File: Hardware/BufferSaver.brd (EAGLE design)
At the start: 12.7 x 17.4 mm, 26 parts, among them U1 SN74AHC1G125, U3 SN74AHC1G125

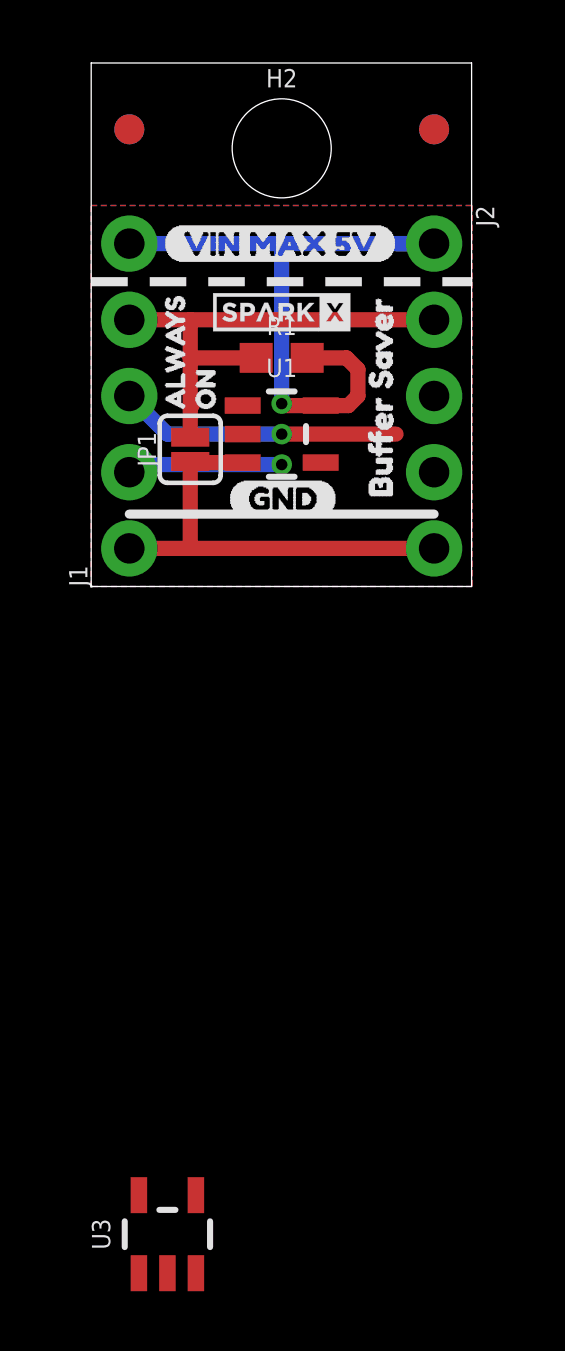
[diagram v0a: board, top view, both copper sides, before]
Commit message: Revert "Added a second buffer to allow for multiple led strips on one SPI port!"
This reverts commit a22a5d977a95e097da70702a3350ebab49920d41.
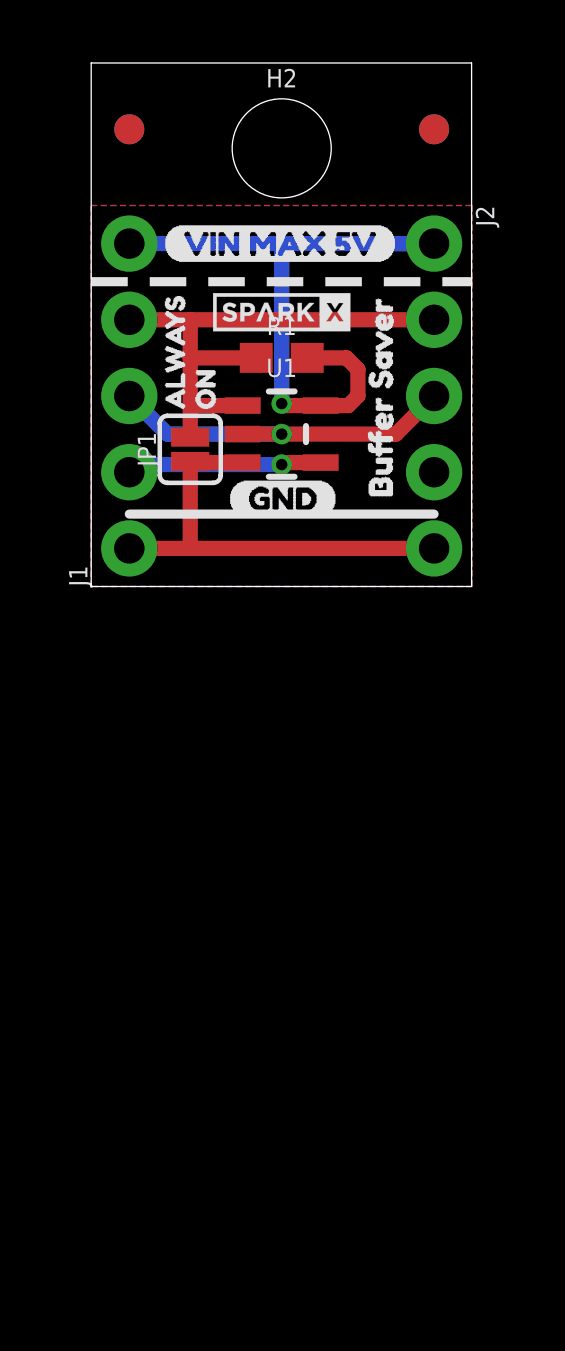
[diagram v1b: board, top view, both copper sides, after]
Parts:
- removed U3: SN74AHC1G125, SparkFun-IC-Logic:SOT23-5
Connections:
- removed net MOSI_IN: J1.3, U1.2, U3.2
- removed net MOSI_OUT: J2.3, U3.4
- new net MOSI: J1.3, J2.3, U1.2
- net !CS: no longer U3.1
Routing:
- net MOSI: track 0.00 -> 12.5 mm, vias 0 -> 1
- net MOSI_IN: track 9.42 -> 0.00 mm, vias 1 -> 0
- net !CS: track 16.4 -> 18.0 mm
- net MISO: track 5.28 -> 6.51 mm
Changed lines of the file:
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@@
 <element name="U$14" library="buzzard_labels" package="VIN_MAX_5V11" value="" x="2.413" y="11.43"/>
 <element name="U$3" library="buzzard_labels" package="VIN_MAX_5V11" value="" x="10.16" y="11.43" rot="MR0"/>
-<element name="U3" library="SparkFun-IC-Logic" package="SOT23-5" value="SN74AHC1G125" x="2.54" y="-21.59">
-<attribute name="PROD_ID" value="IC-11920" x="2.54" y="-21.59" size="1.778" layer="27" font="vector" ratio="15" display="off"/>
-</element>
 </elements>
 <signals>
@@
 <contactref element="J1" pad="4"/>
 <contactref element="J2" pad="2"/>
+<contactref element="U1" pad="1"/>
 <wire x1="1.27" y1="8.89" x2="3.302" y2="8.89" width="0.508" layer="1"/>
 <wire x1="3.302" y1="8.89" x2="11.43" y2="8.89" width="0.508" layer="1"/>
@@
 <wire x1="3.302" y1="5.969" x2="3.302" y2="7.62" width="0.508" layer="1"/>
 <wire x1="3.302" y1="7.62" x2="3.302" y2="8.89" width="0.508" layer="1"/>
+<wire x1="5.0499" y1="6.03" x2="3.363" y2="6.03" width="0.508" layer="1"/>
 <wire x1="3.363" y1="6.03" x2="3.302" y2="5.969" width="0.508" layer="1"/>
 <wire x1="5.5" y1="7.62" x2="3.302" y2="7.62" width="0.508" layer="1"/>
-<contactref element="U1" pad="1"/>
-<contactref element="U3" pad="1"/>
-<wire x1="3.302" y1="4.9784" x2="1.59" y2="-22.8901" width="0" layer="19" extent="1-1"/>
-<wire x1="5.0499" y1="6.03" x2="5.5" y2="7.62" width="0" layer="19" extent="1-1"/>
 </signal>
-<signal name="MOSI_IN">
+<signal name="MOSI">
 <contactref element="J1" pad="3"/>
+<contactref element="U1" pad="2"/>
+<contactref element="J2" pad="3"/>
+<wire x1="11.43" y1="6.35" x2="10.16" y2="5.08" width="0.508" layer="1"/>
+<wire x1="5.0499" y1="5.08" x2="6.35" y2="5.08" width="0.508" layer="1"/>
 <via x="6.35" y="5.08" extent="1-16" drill="0.381"/>
 <wire x1="6.35" y1="5.08" x2="2.54" y2="5.08" width="0.508" layer="16"/>
 <wire x1="2.54" y1="5.08" x2="1.27" y2="6.35" width="0.508" layer="16"/>
 <wire x1="10.16" y1="5.08" x2="6.35" y2="5.08" width="0.508" layer="1"/>
-<contactref element="U1" pad="2"/>
-<contactref element="U3" pad="2"/>
-<wire x1="2.54" y1="5.08" x2="2.54" y2="-22.8901" width="0" layer="19" extent="1-16"/>
-<wire x1="5.0499" y1="5.08" x2="6.35" y2="5.08" width="0" layer="19" extent="1-1"/>
 </signal>
 <signal name="MISO">
+<contactref element="U1" pad="4"/>
 <contactref element="J1" pad="2"/>
 <via x="6.35" y="4.064" extent="1-16" drill="0.381"/>
 <wire x1="6.35" y1="4.064" x2="1.524" y2="4.064" width="0.508" layer="16"/>
 <wire x1="1.524" y1="4.064" x2="1.27" y2="3.81" width="0.508" layer="16"/>
+<wire x1="7.6501" y1="4.13" x2="6.416" y2="4.13" width="0.508" layer="1"/>
 <wire x1="6.416" y1="4.13" x2="6.35" y2="4.064" width="0.508" layer="1"/>
-<contactref element="U1" pad="4"/>
-<wire x1="6.416" y1="4.13" x2="7.6501" y2="4.13" width="0" layer="19" extent="1-1"/>
-</signal>
-<signal name="MOSI_OUT">
-<contactref element="U3" pad="4"/>
-<contactref element="J2" pad="3"/>
-<wire x1="11.43" y1="6.35" x2="3.49" y2="-20.2899" width="0" layer="19" extent="1-1"/>
 </signal>
 </signals>

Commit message: Revert "Revert "Added a second buffer to allow for multiple led strips on one SPI port!""
This reverts commit 93b898f1311a7606d26b6a396d53439853d3f191.
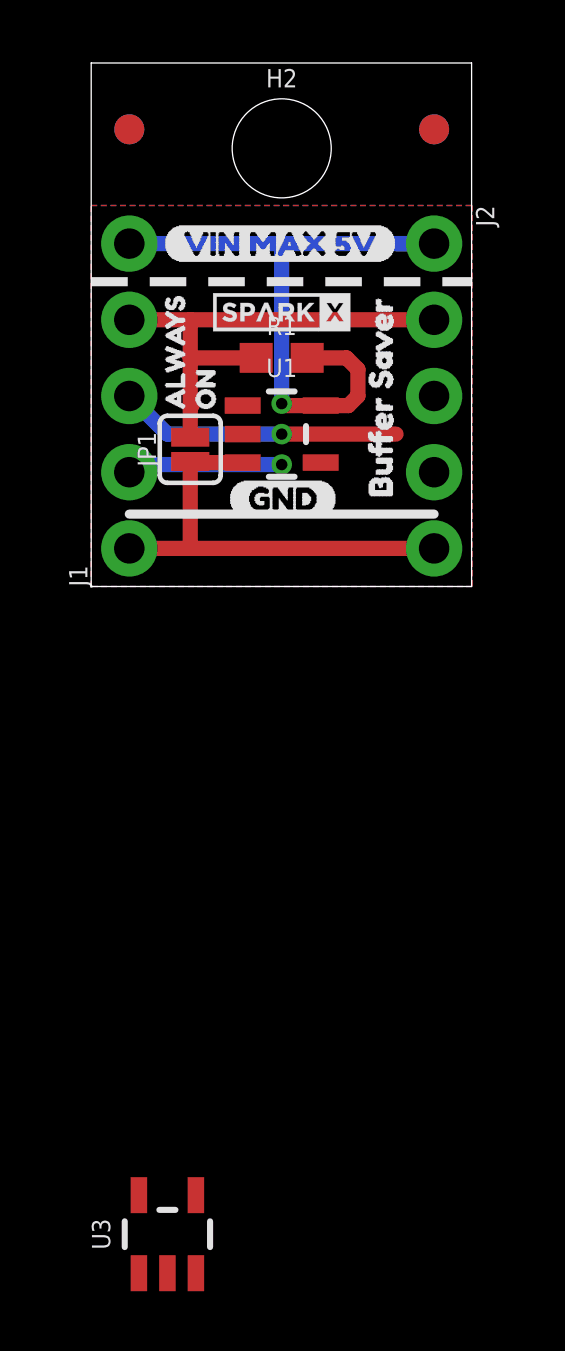
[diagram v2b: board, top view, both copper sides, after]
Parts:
- added U3: SN74AHC1G125, SparkFun-IC-Logic:SOT23-5
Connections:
- removed net MOSI: J1.3, J2.3, U1.2
- new net MOSI_IN: J1.3, U1.2, U3.2
- new net MOSI_OUT: J2.3, U3.4
- net !CS: now also U3.1
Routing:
- net MOSI: track 12.5 -> 0.00 mm, vias 1 -> 0
- net MOSI_IN: track 0.00 -> 9.42 mm, vias 0 -> 1
- net !CS: track 18.0 -> 16.4 mm
- net MISO: track 6.51 -> 5.28 mm
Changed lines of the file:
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@@
 <element name="U$14" library="buzzard_labels" package="VIN_MAX_5V11" value="" x="2.413" y="11.43"/>
 <element name="U$3" library="buzzard_labels" package="VIN_MAX_5V11" value="" x="10.16" y="11.43" rot="MR0"/>
+<element name="U3" library="SparkFun-IC-Logic" package="SOT23-5" value="SN74AHC1G125" x="2.54" y="-21.59">
+<attribute name="PROD_ID" value="IC-11920" x="2.54" y="-21.59" size="1.778" layer="27" font="vector" ratio="15" display="off"/>
+</element>
 </elements>
 <signals>
@@
 <contactref element="J1" pad="4"/>
 <contactref element="J2" pad="2"/>
-<contactref element="U1" pad="1"/>
 <wire x1="1.27" y1="8.89" x2="3.302" y2="8.89" width="0.508" layer="1"/>
 <wire x1="3.302" y1="8.89" x2="11.43" y2="8.89" width="0.508" layer="1"/>
@@
 <wire x1="3.302" y1="5.969" x2="3.302" y2="7.62" width="0.508" layer="1"/>
 <wire x1="3.302" y1="7.62" x2="3.302" y2="8.89" width="0.508" layer="1"/>
-<wire x1="5.0499" y1="6.03" x2="3.363" y2="6.03" width="0.508" layer="1"/>
 <wire x1="3.363" y1="6.03" x2="3.302" y2="5.969" width="0.508" layer="1"/>
 <wire x1="5.5" y1="7.62" x2="3.302" y2="7.62" width="0.508" layer="1"/>
+<contactref element="U1" pad="1"/>
+<contactref element="U3" pad="1"/>
+<wire x1="3.302" y1="4.9784" x2="1.59" y2="-22.8901" width="0" layer="19" extent="1-1"/>
+<wire x1="5.0499" y1="6.03" x2="5.5" y2="7.62" width="0" layer="19" extent="1-1"/>
 </signal>
-<signal name="MOSI">
+<signal name="MOSI_IN">
 <contactref element="J1" pad="3"/>
-<contactref element="U1" pad="2"/>
-<contactref element="J2" pad="3"/>
-<wire x1="11.43" y1="6.35" x2="10.16" y2="5.08" width="0.508" layer="1"/>
-<wire x1="5.0499" y1="5.08" x2="6.35" y2="5.08" width="0.508" layer="1"/>
 <via x="6.35" y="5.08" extent="1-16" drill="0.381"/>
 <wire x1="6.35" y1="5.08" x2="2.54" y2="5.08" width="0.508" layer="16"/>
 <wire x1="2.54" y1="5.08" x2="1.27" y2="6.35" width="0.508" layer="16"/>
 <wire x1="10.16" y1="5.08" x2="6.35" y2="5.08" width="0.508" layer="1"/>
+<contactref element="U1" pad="2"/>
+<contactref element="U3" pad="2"/>
+<wire x1="2.54" y1="5.08" x2="2.54" y2="-22.8901" width="0" layer="19" extent="1-16"/>
+<wire x1="5.0499" y1="5.08" x2="6.35" y2="5.08" width="0" layer="19" extent="1-1"/>
 </signal>
 <signal name="MISO">
-<contactref element="U1" pad="4"/>
 <contactref element="J1" pad="2"/>
 <via x="6.35" y="4.064" extent="1-16" drill="0.381"/>
 <wire x1="6.35" y1="4.064" x2="1.524" y2="4.064" width="0.508" layer="16"/>
 <wire x1="1.524" y1="4.064" x2="1.27" y2="3.81" width="0.508" layer="16"/>
-<wire x1="7.6501" y1="4.13" x2="6.416" y2="4.13" width="0.508" layer="1"/>
 <wire x1="6.416" y1="4.13" x2="6.35" y2="4.064" width="0.508" layer="1"/>
+<contactref element="U1" pad="4"/>
+<wire x1="6.416" y1="4.13" x2="7.6501" y2="4.13" width="0" layer="19" extent="1-1"/>
+</signal>
+<signal name="MOSI_OUT">
+<contactref element="U3" pad="4"/>
+<contactref element="J2" pad="3"/>
+<wire x1="11.43" y1="6.35" x2="3.49" y2="-20.2899" width="0" layer="19" extent="1-1"/>
 </signal>
 </signals>
